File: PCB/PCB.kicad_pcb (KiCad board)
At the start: 2 copper layers, 53.3 x 73.7 mm, 23 parts, among them J1 PWR,A0, J10 D8-D10, J11 D0-D7, J12 GrowLight Out, J2 12V, J3 LightSensor, J4 Pump1, J5 Sensor1, J6 GrowLight In, J7 Pump2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

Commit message: Kicad-files for MivinDrivhus_v5
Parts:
- added J13: Pump3, TerminalBlock:TerminalBlock_bornier-2_P5.08mm, F.Cu at (177.8, 128.3)
- added J14: Sensor3, TerminalBlock:TerminalBlock_bornier-3_P5.08mm, F.Cu at (182.9, 59.7)
- added K4: Relay3, Relay_THT:Relay_SPDT_SANYOU_SRD_Series_Form_C, F.Cu at (180.3, 105.4)
- added Q4: BC337, Package_TO_SOT_THT:TO-92_Inline, F.Cu at (172.7, 99.1)
- added R4: 1K, Resistor_THT:R_Axial_DIN0207_L6.3mm_D2.5mm_P10.16mm_Horizontal, F.Cu at (158.8, 64.8)
- added R5: 1K, Resistor_THT:R_Axial_DIN0207_L6.3mm_D2.5mm_P10.16mm_Horizontal, F.Cu at (157.5, 86.4)
- J2: value 12V -> Pump In; footprint TerminalBlock:TerminalBlock_bornier-2_P5.08mm -> Connector_BarrelJack:BarrelJack_Wuerth_6941xx301002
- U1: value AM2302 -> DHT11
- moved J2 57.8 mm to (153.7, 96.5), turned to 270 degrees
- moved J5 41.3 mm to (182.9, 97.8), turned to 90 degrees
- moved R3 28.2 mm to (157.5, 90.2), turned to 0 degrees
- moved J8 26.8 mm to (182.9, 78.7), turned to 90 degrees
- moved J4 26.5 mm to (144.8, 128.3)
- moved J9 25.9 mm to (165.1, 59.7), turned to 270 degrees
- moved K1 25.9 mm to (147.3, 105.4)
- moved K3 25.9 mm to (163.8, 105.4)
- moved J7 24.3 mm to (161.3, 128.3)
- moved Q3 21.0 mm to (166.4, 99.1)
- moved K2 19.6 mm to (162.9, 54.0), turned to 90 degrees
- moved Q2 15.5 mm to (174.0, 45.7)
- moved R2 15.5 mm to (174.0, 52.1)
- moved U1 15.2 mm to (147.1, 53.3), turned to 0 degrees
- moved Q1 12.1 mm to (160.0, 99.1)
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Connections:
- J1 pad 5: +12V -> (no net)
- J10 pad 2: (no net) -> Net-(J10-Pad2)
- J2 pad 1: GND -> Net-(J13-Pad1)
- J2 pad 2: +12V -> Net-(J2-Pad2)
- J4 pad 1: GND -> Net-(J13-Pad1)
- J7 pad 1: GND -> Net-(J13-Pad1)
- K1 pad 1: +12V -> Net-(J2-Pad2)
- K3 pad 1: +12V -> Net-(J2-Pad2)
- R2 pad 2: Net-(J10-Pad3) -> Net-(J10-Pad2)
- U2 pad 12: (no net) -> Net-(J14-Pad3)
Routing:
- net Net-(J13-Pad1): track 0.00 -> 89.9 mm
- net +12V: track 78.3 -> 0.00 mm
- net Net-(J2-Pad2): track 0.00 -> 54.2 mm
- net Net-(J8-Pad3): track 76.3 -> 25.5 mm
- net Net-(J5-Pad3): track 78.4 -> 33.3 mm, vias 3 -> 2
- net Net-(J11-Pad6): track 58.4 -> 98.9 mm, vias 1 -> 6
- net GND: track 210.4 -> 174.9 mm, vias 0 -> 2
- net Net-(J14-Pad3): track 0.00 -> 27.9 mm
- net Net-(J10-Pad2): track 0.00 -> 27.3 mm, vias 0 -> 1
- net Net-(J11-Pad2): track 47.9 -> 26.0 mm, vias 1 -> 0
- net Net-(J11-Pad1): track 5.08 -> 25.5 mm
- net Net-(Q4-Pad2): track 0.00 -> 20.3 mm
- net +5V: track 108.7 -> 128.7 mm, vias 0 -> 1
- net Net-(K3-Pad2): track 30.9 -> 13.1 mm
- net Net-(J12-Pad2): track 13.4 -> 29.9 mm
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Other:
- board size 53.3 x 73.7 mm -> 53.3 x 96.5 mm
- board text added: "- +"
- board text added: "MiniDrivhus v5"
- board text added: "Pump3"
- board text added: "Sensor3"
- board text removed: "12V"
- board text removed: "3V 5V GND GND 12V A0"
- board text removed: "D10 D9 D8"
- board text removed: "D7 D6 D5 D4 D3 D2 D1 D0"
- board text removed: "GrowLight Relay"
- board text removed: "MiniDrivhus v4"
- board text removed: "Plant 1 Relay"
- board text removed: "Plant 2 Relay"

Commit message: PCB v5.1
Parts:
- Q1, Q2, Q3, Q4: footprint Package_TO_SOT_THT:TO-92_Inline -> Package_TO_SOT_THT:TO-92_HandSolder
- moved Q1 2.62 mm to (157.5, 99.7), turned to 0 degrees
- moved Q3 2.62 mm to (163.8, 99.7), turned to 0 degrees
- moved Q4 2.62 mm to (170.2, 99.7), turned to 0 degrees
- moved U2 1.19 mm to (166.4, 74.9)
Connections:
- J10 pad 1: (no net) -> Net-(J10-Pad1)
- J10 pad 2: Net-(J10-Pad2) -> (no net)
- R2 pad 2: Net-(J10-Pad2) -> Net-(J10-Pad1)
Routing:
- net Net-(J10-Pad2): track 27.3 -> 0.00 mm, vias 1 -> 0
- net Net-(J10-Pad1): track 0.00 -> 24.0 mm, vias 0 -> 1
- net Net-(K2-Pad2): track 18.2 -> 8.81 mm
- net +3V3: track 90.0 -> 94.8 mm, vias 2 -> 1
- net Net-(K1-Pad2): track 25.8 -> 22.0 mm
- net Net-(K3-Pad2): track 13.1 -> 10.2 mm
- net Net-(J11-Pad3): track 44.3 -> 42.1 mm
- net Net-(Q2-Pad2): track 7.40 -> 5.61 mm
- net Net-(J8-Pad3): track 25.5 -> 26.9 mm
- net GND: track 174.9 -> 173.6 mm
- net Net-(Q4-Pad2): track 20.3 -> 19.0 mm
- net Net-(J11-Pad6): track 98.9 -> 99.9 mm
- net Net-(J1-Pad7): track 25.0 -> 25.9 mm
- net Net-(Q3-Pad2): track 12.0 -> 11.4 mm
- net Net-(Q1-Pad2): track 5.61 -> 4.97 mm
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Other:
- board text added: "1"
- board text added: "2"
- board text added: "3"
- board text added: "MiniDrivhus v5.1"
- board text removed: "MiniDrivhus v5"

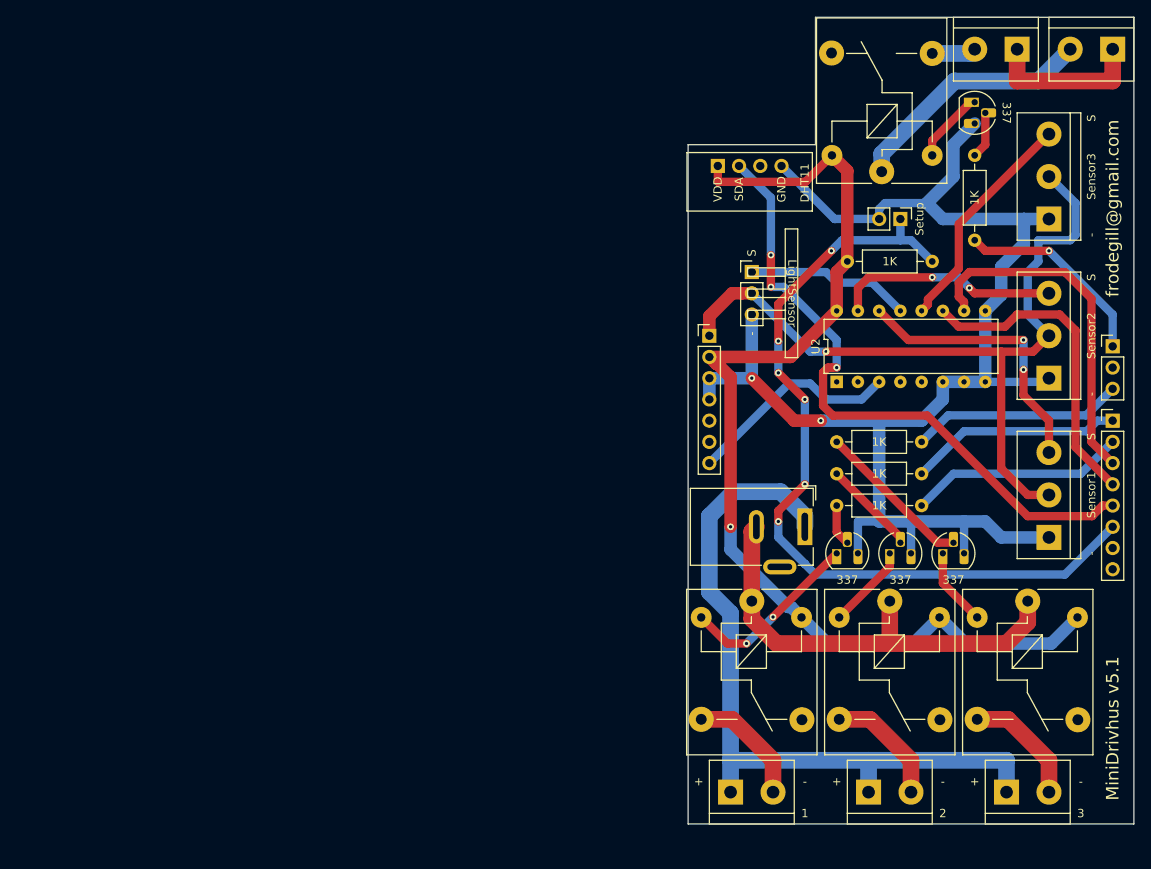
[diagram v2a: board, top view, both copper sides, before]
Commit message: Added support for the fan relay
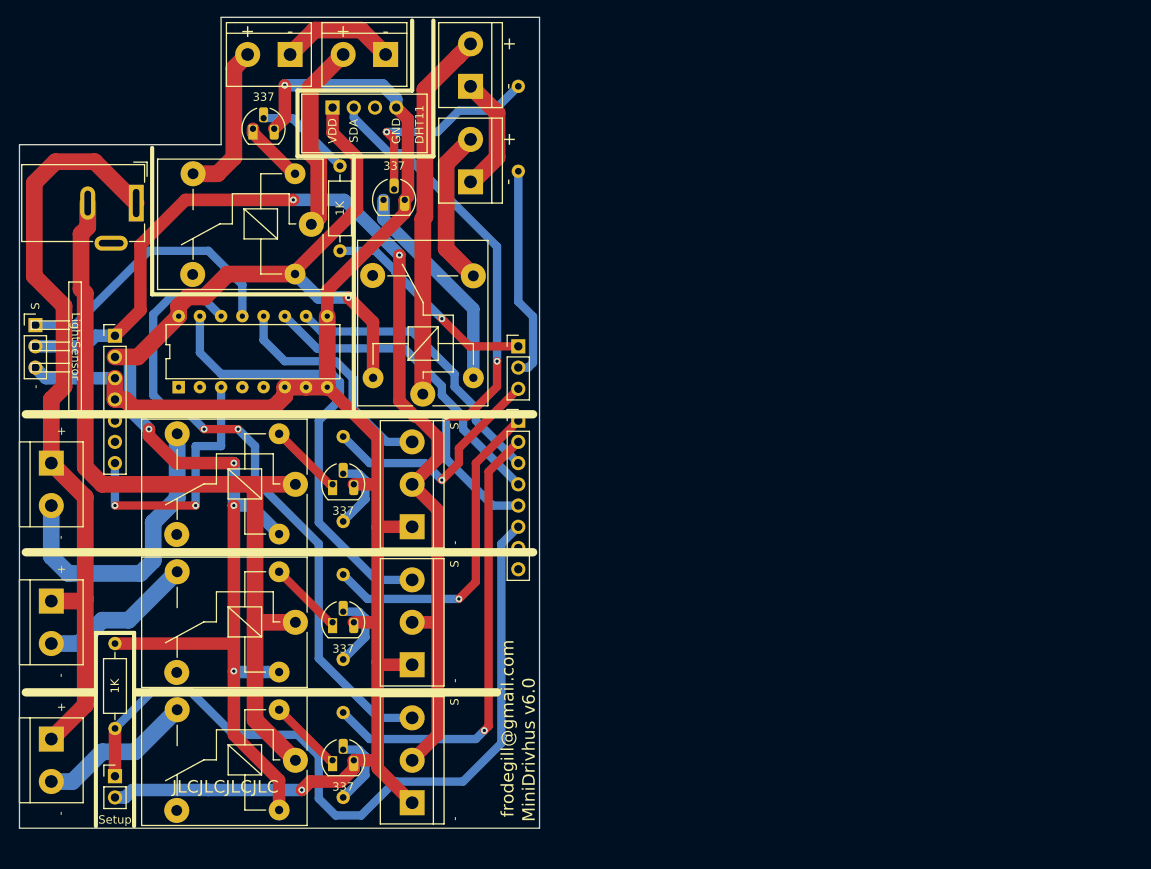
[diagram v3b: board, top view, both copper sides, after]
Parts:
- added 1K: 1K, Resistor_THT:R_Axial_DIN0207_L6.3mm_D2.5mm_P10.16mm_Horizontal, B.Cu at (119.4, 43.8)
- added 337: BC337, Package_TO_SOT_THT:TO-92_HandSolder, F.Cu at (103.3, 57.4)
- added J15: Fan In, TerminalBlock:TerminalBlock_bornier-2_P5.08mm, F.Cu at (113.7, 55.2)
- added J16: Fan Out, TerminalBlock:TerminalBlock_bornier-2_P5.08mm, F.Cu at (113.7, 43.8)
- added K5: RelayFan, Relay_THT:Relay_SPDT_SANYOU_SRD_Series_Form_C, F.Cu at (108.0, 80.6)
- R1, R3, R5: moved to B.Cu
- moved J13 120.9 mm to (63.5, 88.9), turned to 270 degrees
- moved J9 115.2 mm to (71.1, 126.4), turned to 0 degrees
- moved J7 100.4 mm to (63.5, 105.4), turned to 270 degrees
- moved R4 98.8 mm to (71.1, 110.5), turned to 270 degrees
- moved J2 88.9 mm to (73.7, 57.8)
- moved K4 88.7 mm to (92.7, 91.4), turned to 180 degrees
- moved J12 87.0 mm to (103.5, 40.0)
- moved J6 87.0 mm to (92.1, 40.0)
- moved Q2 86.4 mm to (87.6, 48.9), turned to 0 degrees
- moved J3 86.0 mm to (61.6, 74.9)
- moved J14 84.6 mm to (106.7, 96.5)
- moved J8 83.6 mm to (106.7, 113.0)
- moved J5 82.5 mm to (106.7, 129.5)
- moved J4 81.5 mm to (63.5, 121.9), turned to 270 degrees
- moved U2 78.7 mm to (87.6, 75.6)
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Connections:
- J10 pad 2: (no net) -> Net-(J10-Pad2)
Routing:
- net Net-(J16-Pad2): track 0.00 -> 44.3 mm
- net Net-(J2-Pad2): track 54.2 -> 98.1 mm
- net Net-(J5-Pad3): track 33.4 -> 76.9 mm
- net +5V: track 128.5 -> 162.7 mm, vias 1 -> 5
- net +3V3: track 94.8 -> 127.6 mm, vias 1 -> 2
- net Net-(J11-Pad2): track 26.0 -> 54.9 mm, vias 0 -> 1
- net Net-(J8-Pad3): track 26.9 -> 54.5 mm, vias 2 -> 0
- net GND: track 173.6 -> 200.9 mm
- net Net-(K5-Pad2): track 0.00 -> 25.7 mm
- net Net-(J10-Pad2): track 0.00 -> 25.7 mm
- net Net-(Q5-Pad2): track 0.00 -> 25.2 mm, vias 0 -> 1
- net Net-(J13-Pad2): track 14.4 -> 36.1 mm
- net Net-(J15-Pad2): track 0.00 -> 18.9 mm
- net Net-(J15-Pad1): track 0.00 -> 14.2 mm
- net Net-(J3-Pad1): track 19.7 -> 33.9 mm
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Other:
- board size 53.3 x 96.5 mm -> 62.2 x 97 mm
- board text added: "Fan"
- board text added: "Fan In"
- board text added: "Fan Out"
- board text added: "GrowLight"
- board text added: "JLCJLCJLCJLC"
- board text added: "MiniDrivhus v6.0"
- board text added: "Plant1"
- board text added: "Plant2"
- board text added: "Plant3"
- board text added: "Pump"
- board text added: "Pumps In"
- board text added: "Sensor"
- board text removed: "1"
- board text removed: "2"
- board text removed: "3"
- board text removed: "MiniDrivhus v5.1"
- board text removed: "Pump1"
- board text removed: "Pump2"
- board text removed: "Pump3"
- board text removed: "Sensor1"
- board text removed: "Sensor2"
- board text removed: "Sensor3"

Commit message: Added fan support to minidrivhus
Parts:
- removed 1K: 1K, Resistor_THT:R_Axial_DIN0207_L6.3mm_D2.5mm_P10.16mm_Horizontal
- removed 337: BC337, Package_TO_SOT_THT:TO-92_HandSolder
- added Q5: BC337, Package_TO_SOT_THT:TO-92_HandSolder, F.Cu at (103.3, 57.4)
- added R6: 10K, Resistor_THT:R_Axial_DIN0207_L6.3mm_D2.5mm_P10.16mm_Horizontal, F.Cu at (119.4, 43.8)
- added R7: 10K, Resistor_THT:R_Axial_DIN0207_L6.3mm_D2.5mm_P10.16mm_Horizontal, F.Cu at (106.7, 60.3)
- added R8: 10K, Resistor_THT:R_Axial_DIN0207_L6.3mm_D2.5mm_P10.16mm_Horizontal, B.Cu at (114.9, 116.2)
- R2, R5: value 1K -> 10K
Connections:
- J1 pad 5: (no net) -> unconnected-(J1-Pad5)
- J1 pad 6: (no net) -> unconnected-(J1-Pad6)
- J11 pad 7: (no net) -> unconnected-(J11-Pad7)
- J11 pad 8: (no net) -> unconnected-(J11-Pad8)
- K1 pad 4: (no net) -> unconnected-(K1-Pad4)
- K2 pad 4: (no net) -> unconnected-(K2-Pad4)
- K3 pad 4: (no net) -> unconnected-(K3-Pad4)
- K4 pad 4: (no net) -> unconnected-(K4-Pad4)
- K5 pad 4: (no net) -> unconnected-(K5-Pad4)
- U1 pad 3: (no net) -> unconnected-(U1-Pad3)
- U2 pad 1: (no net) -> unconnected-(U2-Pad1)
- U2 pad 2: (no net) -> unconnected-(U2-Pad2)
- U2 pad 4: (no net) -> unconnected-(U2-Pad4)
- U2 pad 5: (no net) -> unconnected-(U2-Pad5)
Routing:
- net +5V: track 162.7 -> 188.0 mm, vias 5 -> 6
- net Net-(J10-Pad3): track 28.7 -> 45.7 mm
- net Net-(J10-Pad1): track 26.2 -> 41.8 mm
- net GND: track 200.9 -> 202.6 mm
- net Net-(J11-Pad2): track 54.9 -> 56.2 mm
- net Net-(J15-Pad2): track 18.9 -> 20.2 mm
- net Net-(J16-Pad2): track 44.3 -> 45.1 mm
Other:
- board size 62.2 x 97 mm -> 62.5 x 97 mm
- net class Default removed
- board text added: "MiniDrivhus v6.1"
- board text removed: "MiniDrivhus v6.0"
